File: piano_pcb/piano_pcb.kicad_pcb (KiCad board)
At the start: 2 copper layers, 115 x 85 mm, 28 parts, among them J1 DIN-6, J2 DIN-6, J3 Conn_02x06_Odd_Even, J4 Arduino-NANO-33, J5 SWD, J6 Conn_02x01, U1 TB6612FNG, U2 CN3302_module, U3 battery_holder, U4 MCP1700-1202E_TO92

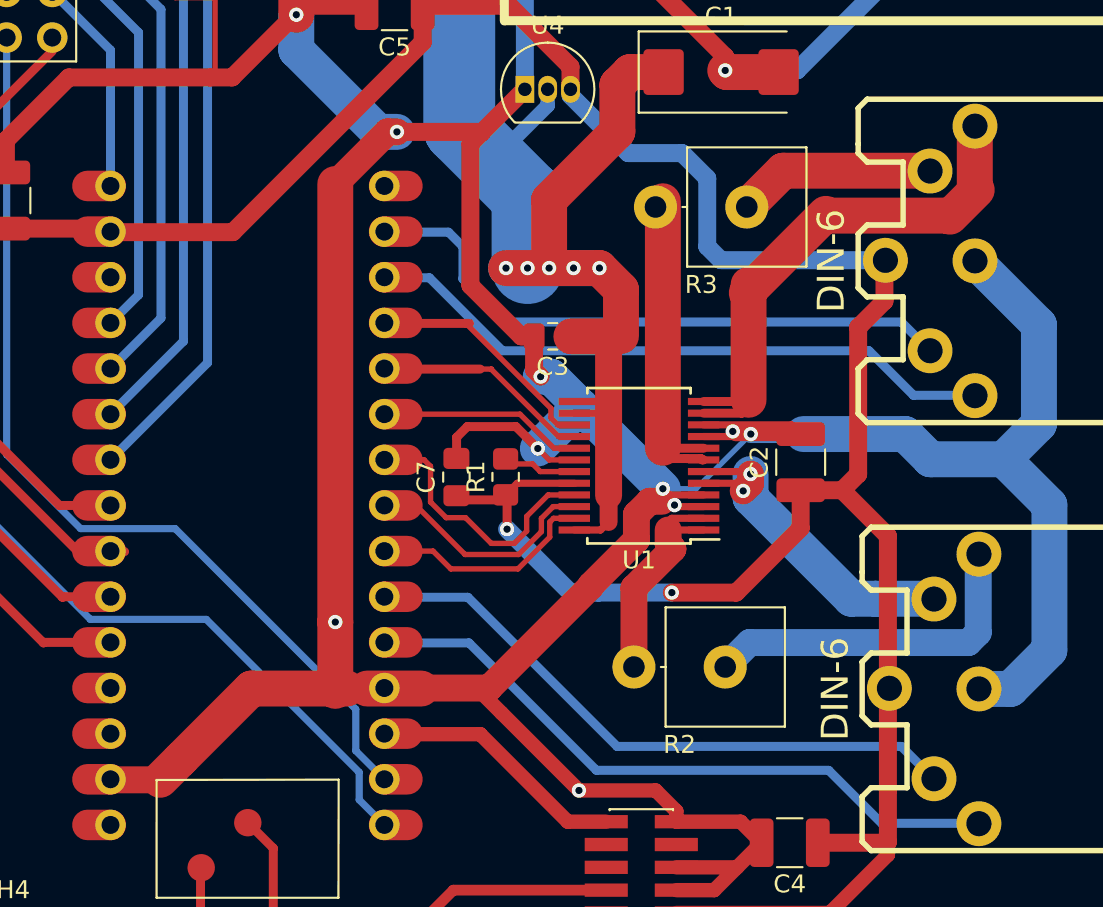
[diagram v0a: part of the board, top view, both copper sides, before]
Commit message: Updated schematics, NOT PCB
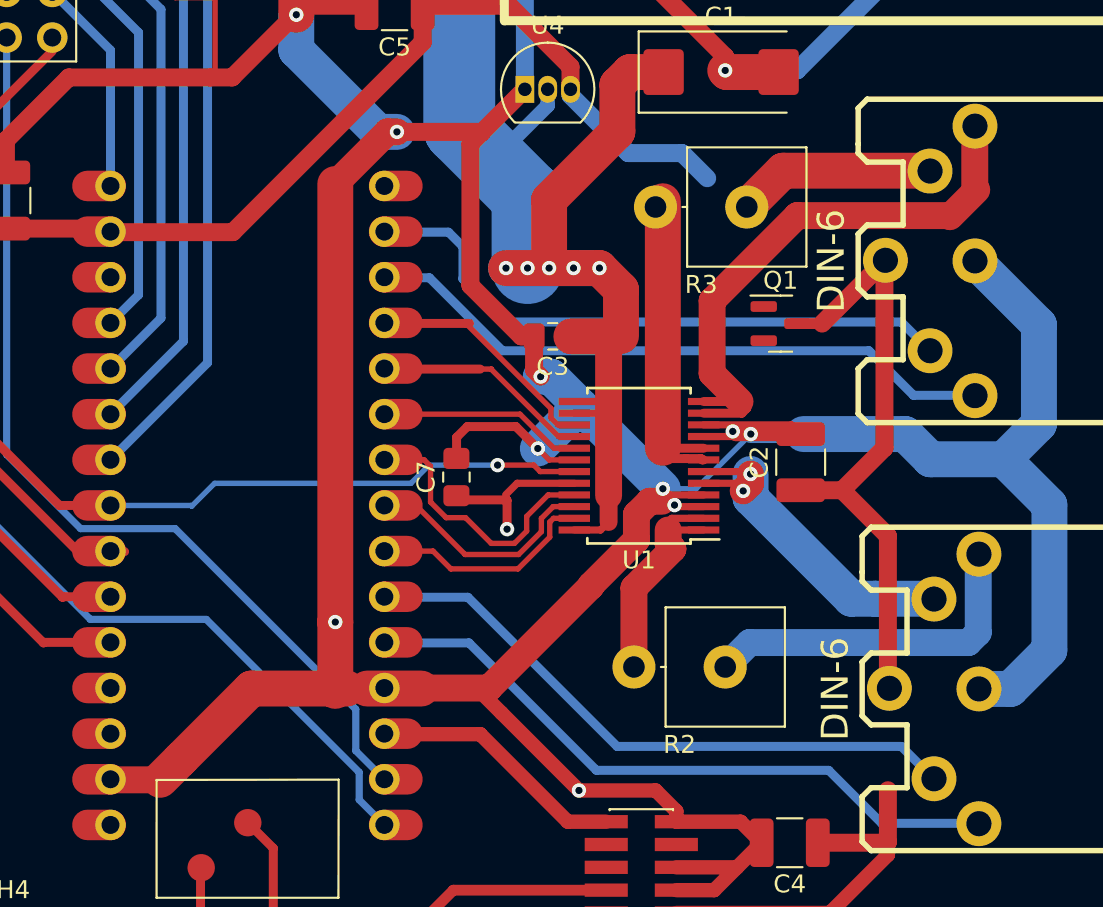
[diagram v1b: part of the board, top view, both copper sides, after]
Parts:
- removed R1: 10k, Resistor_SMD:R_0805_2012Metric_Pad1.20x1.40mm_HandSolder
- added Q1: FDN340P, Package_TO_SOT_SMD:SOT-23, F.Cu at (182.9, 110.5)
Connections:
- C2 pad 1: +3V3 -> Net-(J1-Pad3)
- J1 pad 3: +3V3 -> Net-(J1-Pad3)
- J2 pad 3: +3V3 -> Net-(J1-Pad3)
- J3 pad 12: Net-(J3-Pad12) -> /Controller/stby
- J4 pad 12: Net-(J4-Pad12) -> unconnected-(J4-Pad12)
- J4 pad 13: Net-(J4-Pad13) -> unconnected-(J4-Pad13)
- J4 pad 15: Net-(J4-Pad15) -> unconnected-(J4-Pad15)
- J4 pad 3: Net-(J4-Pad3) -> unconnected-(J4-Pad3)
- J4 pad 30: Net-(J4-Pad30) -> /Controller/EncV3.3
- J4 pad 8: Net-(J3-Pad12) -> /Controller/stby
- J5 pad 6: Net-(J5-Pad6) -> unconnected-(J5-Pad6)
- J5 pad 7: Net-(J5-Pad7) -> unconnected-(J5-Pad7)
- J5 pad 8: Net-(J5-Pad8) -> unconnected-(J5-Pad8)
- U1 pad 19: Net-(R1-Pad2) -> /Controller/stby
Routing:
- net +3V3: track 175.9 -> 106.7 mm, vias 3 -> 2
- net /Controller/stby: track 0.00 -> 61.0 mm, vias 0 -> 1
- net Net-(J1-Pad3): track 0.00 -> 34.8 mm
- net Net-(J3-Pad12): track 34.1 -> 0.00 mm
- net Net-(R1-Pad2): track 3.95 -> 0.00 mm
- net Net-(J1-Pad1): track 30.0 -> 32.1 mm

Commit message: Updated firmware and app
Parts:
- added J7: Conn_01x02, TerminalBlock_Altech:Altech_AK300_1x02_P5.00mm_45-Degree, F.Cu at (155.0, 73.7)
- C1: value 100u -> 10u
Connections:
- C2 pad 1: Net-(J1-Pad3) -> +3V3
- J1 pad 3: Net-(J1-Pad3) -> Net-(Q1-D)
- J2 pad 3: Net-(J1-Pad3) -> Net-(Q1-D)
- Q1 pad 3: Net-(J1-Pad3) -> Net-(Q1-D)
- U2 pad 2: /Controller/Bat -> Net-(J7-Pin_1)
- U3 pad 3: /Controller/Bat -> Net-(J7-Pin_1)
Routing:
- net GND: track 443.3 -> 250.6 mm, vias 11 -> 8
- net /Controller/Bat: track 143.0 -> 19.2 mm, vias 6 -> 0
- net Net-(J1-Pad3): track 34.8 -> 0.00 mm
- net +3V3: track 106.7 -> 141.5 mm
- removed copper zone on B.Cu, net GND

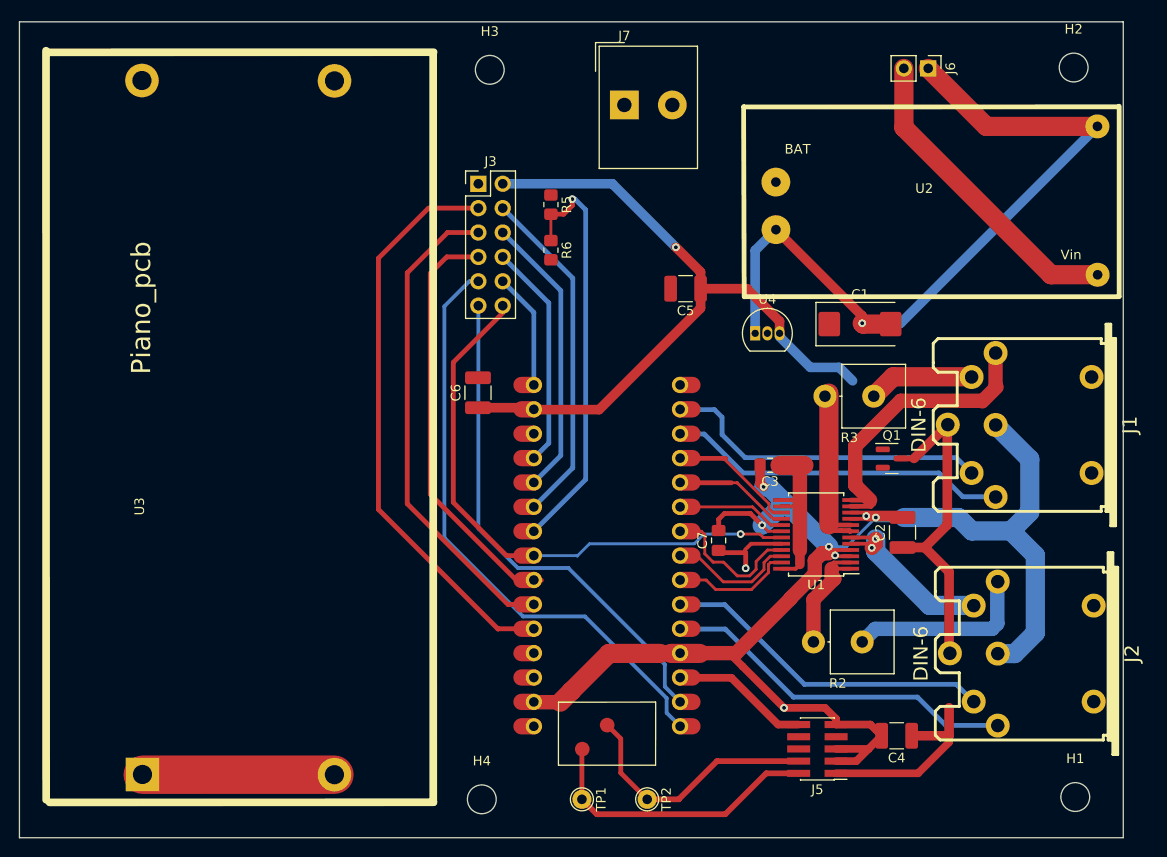
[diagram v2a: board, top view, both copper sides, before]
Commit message: Optimized for low power
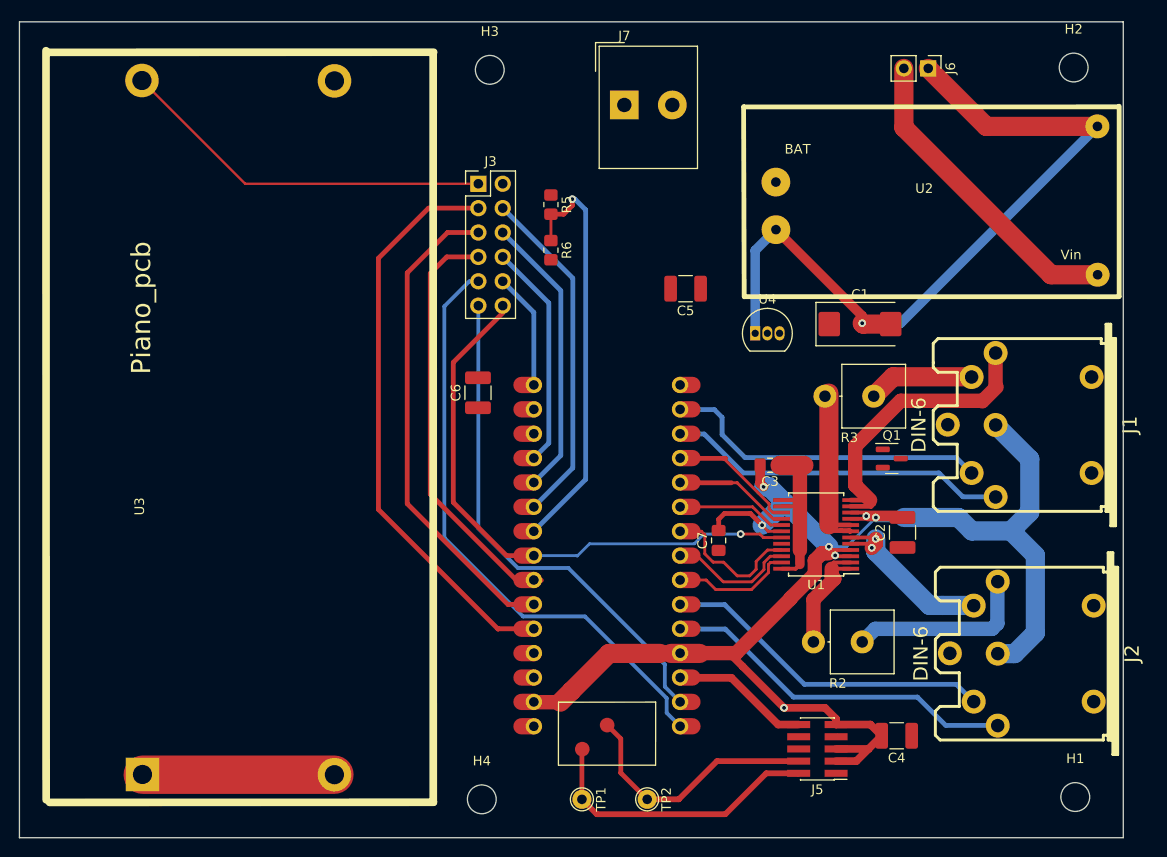
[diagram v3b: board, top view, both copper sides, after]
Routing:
- net +3V3: track 141.5 -> 0.00 mm, vias 2 -> 0
- net GND: track 250.6 -> 290.1 mm

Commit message: PCB to version 2.0
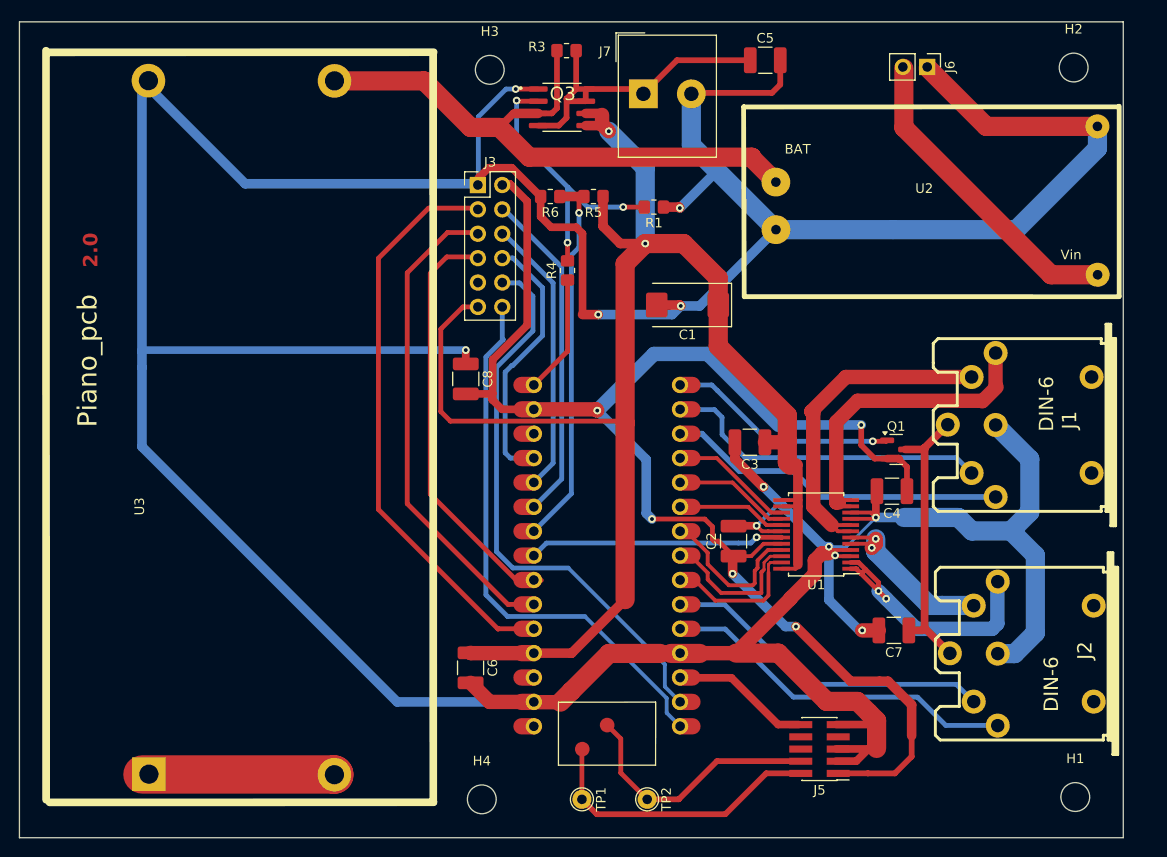
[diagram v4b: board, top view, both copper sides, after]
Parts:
- removed R2: 1, Resistor_THT:R_Axial_Power_L20.0mm_W6.4mm_P5.08mm_Vertical
- removed U4: MCP1700-1202E_TO92, Package_TO_SOT_THT:TO-92_Inline
- added C8: 100n, Capacitor_SMD:C_1210_3225Metric_Pad1.33x2.70mm_HandSolder, F.Cu at (138.5, 102.2)
- added Q3: IRF7319, library:SOIC127P600X175-8N, F.Cu at (148.5, 73.9)
- added R1: 10k, Resistor_SMD:R_0805_2012Metric_Pad1.20x1.40mm_HandSolder, F.Cu at (158.1, 84.3)
- added R4: 100, Resistor_SMD:R_0805_2012Metric_Pad1.20x1.40mm_HandSolder, F.Cu at (149.1, 90.9)
- C1: footprint Capacitor_Tantalum_SMD:CP_EIA-7343-30_AVX-N_Pad2.25x2.55mm_HandSolder -> Capacitor_Tantalum_SMD:CP_EIA-7343-30_AVX-N_HandSolder
- C3, C7: footprint Capacitor_SMD:C_0805_2012Metric_Pad1.18x1.45mm_HandSolder -> Capacitor_SMD:C_1210_3225Metric_Pad1.33x2.70mm_HandSolder
- C4, C6: value 10u -> 100n
- C5: value 10u -> 10n
- J1, J2: footprint myAV:din-6-1cm -> library:din-6-1cm
- J4: footprint myAV:NANO_33_BLE -> library:NANO_33_BLE
- R3: value 1 -> 100k; footprint Resistor_THT:R_Axial_Power_L20.0mm_W6.4mm_P5.08mm_Vertical -> Resistor_SMD:R_0805_2012Metric_Pad1.20x1.40mm_HandSolder
- R5: value 470k -> 220k
- R6: value 330k -> 150k
- U1: footprint myAV:SSOP-24_5.3x8.2mm_P0.65mm -> library:SSOP-24_5.3x8.2mm_P0.65mm
- U2: footprint myAV:CN3302-FP -> library:CN3302-FP
- U3: footprint myAV:Battery_2x_18650 -> library:Battery_2x_18650
- moved R3 48.2 mm to (149.0, 68.0)
- moved C6 28.7 mm to (139.0, 132.3), turned to -90 degrees
- moved C4 25.5 mm to (182.9, 113.9)
- moved C5 25.2 mm to (169.7, 69.0), turned to 0 degrees
- moved C7 20.5 mm to (183.1, 128.4), turned to 180 degrees
- moved C1 18.1 mm to (161.6, 94.5), turned to 180 degrees
- moved C2 17.6 mm to (166.4, 119.1)
- moved R6 5.59 mm to (147.3, 83.2), turned to 180 degrees
- moved R5 4.51 mm to (151.8, 83.2), turned to 180 degrees
- moved C3 3.19 mm to (168.1, 108.8)
- moved J7 2.29 mm to (157.0, 72.5)
- moved Q1 1.05 mm to (183.3, 109.5)
- moved J5 0.22 mm to (175.3, 140.8)
- moved J6 0.18 mm to (186.6, 69.7)
- moved J3 0.14 mm to (139.8, 82.0)
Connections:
- C5 pad 1: +3V3 -> Net-(J7-Pin_1)
- C6 pad 1: +3V3 -> /Controller/Bat
- C7 pad 1: +3V3 -> Net-(Q1-D)
- J3 pad 11: Net-(J3-Pin_11) -> /Controller/Bat
- J3 pad 12: /Controller/stby -> Net-(J3-Pin_12)
- J3 pad 9: Net-(J3-Pin_9) -> unconnected-(J3-Pin_9-Pad9)
- J4 pad 1: Net-(J3-Pin_10) -> /Controller/PPio
- J4 pad 12: unconnected-(J4-Pad12) -> /Controller/Bat
- J4 pad 16: Net-(J3-Pin_9) -> Net-(J3-Pin_12)
- J4 pad 17: Net-(J3-Pin_11) -> Net-(J3-Pin_10)
- J7 pad 2: /Controller/Bat -> GND
- R3 pad 1: Net-(J1-Pad2) -> Net-(J7-Pin_1)
- R3 pad 2: Net-(R3-Pad2) -> Net-(U2-BAT)
- U1 pad 1: Net-(R2-Pad2) -> Net-(J2-Pad1)
- U1 pad 2: Net-(R2-Pad2) -> Net-(J2-Pad1)
- U1 pad 7: Net-(R3-Pad2) -> Net-(J1-Pad2)
- U1 pad 8: Net-(R3-Pad2) -> Net-(J1-Pad2)
- U2 pad 2: Net-(J7-Pin_1) -> Net-(U2-BAT)
- U3 pad 3: Net-(J7-Pin_1) -> Net-(U2-BAT)
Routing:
- net GND: track 290.1 -> 516.0 mm, vias 8 -> 11
- net +3V3: track 0.00 -> 153.8 mm, vias 0 -> 5
- net /Controller/Bat: track 19.2 -> 168.2 mm, vias 0 -> 2
- net Net-(U2-BAT): track 0.00 -> 63.2 mm
- net Net-(J3-Pin_9): track 62.3 -> 0.00 mm
- net Net-(J3-Pin_12): track 0.00 -> 58.3 mm
- net Net-(J3-Pin_11): track 53.1 -> 0.00 mm
- net Net-(J3-Pin_10): track 12.1 -> 58.9 mm
- net /Controller/stby: track 61.0 -> 28.0 mm
- net Net-(J7-Pin_1): track 0.00 -> 32.3 mm
- net Net-(Q3-Pad2): track 0.00 -> 30.2 mm, vias 0 -> 3
- net Net-(Q1-D): track 0.00 -> 29.8 mm
- net Net-(J1-Pad2): track 11.0 -> 35.1 mm
- net /Controller/EncV3.3: track 0.00 -> 24.0 mm, vias 0 -> 1
- net Net-(R3-Pad2): track 18.5 -> 0.00 mm
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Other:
- board text added: "2.0"

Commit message: Updated and added 3d picture
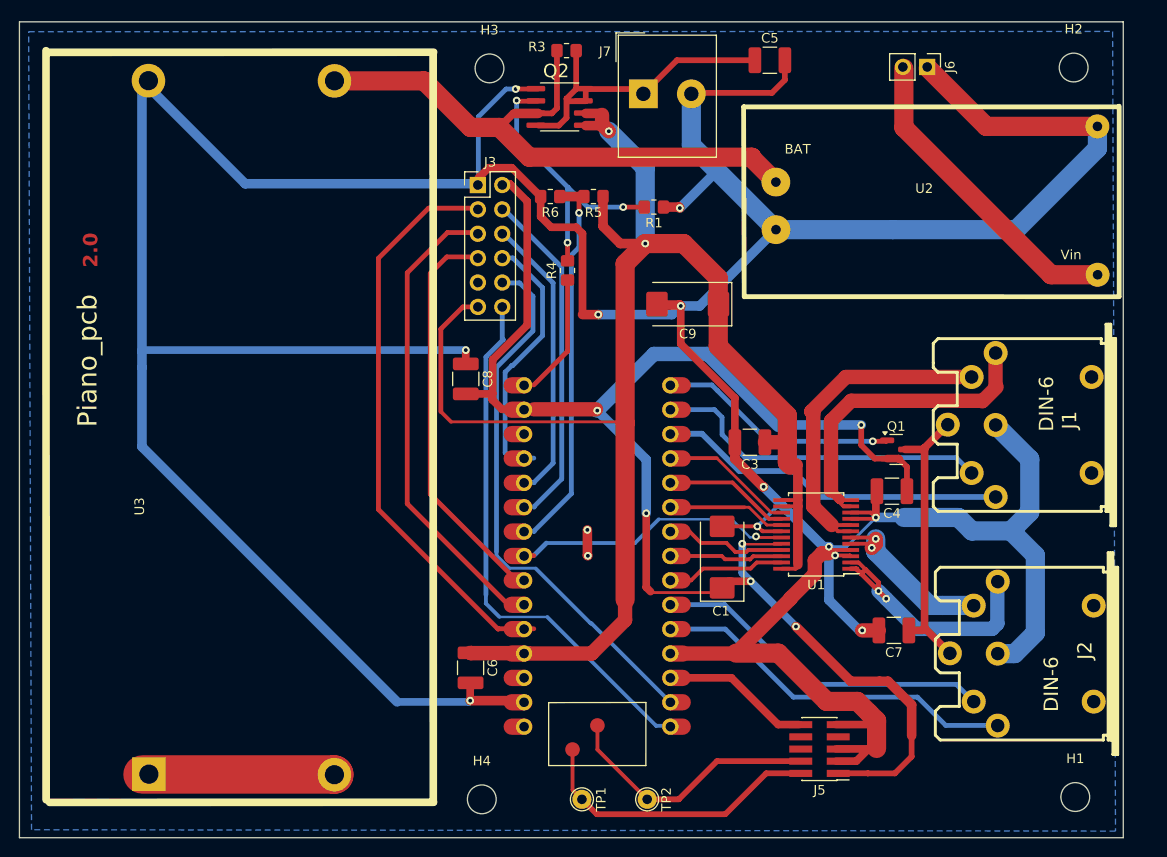
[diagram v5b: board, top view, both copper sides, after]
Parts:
- removed C2: 10u, Capacitor_SMD:C_1210_3225Metric_Pad1.33x2.70mm_HandSolder
- removed J4: Arduino-NANO-33, library:NANO_33_BLE
- removed Q3: IRF7319, library:SOIC127P600X175-8N
- added C9: 10u, Capacitor_Tantalum_SMD:CP_EIA-7343-30_AVX-N_HandSolder, F.Cu at (161.6, 94.4)
- added J8: Arduino-NANO-33, library:NANO_33_BLE, F.Cu at (152.2, 120.7)
- added Q2: IRF7319, library:SOIC127P600X175-8N, F.Cu at (148.3, 73.9)
- moved C1 26.5 mm to (165.2, 120.8), turned to 90 degrees
- moved C5 0.48 mm to (170.2, 69.0)
- moved H3 0.15 mm to (141.0, 69.8)
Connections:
- net Net-(J7-Pin_1) renamed /Power/Vgate
- C1 pad 1: /Controller/Bat -> +3.3V
- C4 pad 1: +3V3 -> +3.3V
- C8 pad 2: +3V3 -> +3.3V
- J3 pad 2: +3V3 -> +3.3V
- J5 pad 1: +3V3 -> +3.3V
- Q1 pad 2: +3V3 -> +3.3V
- U1 pad 20: +3V3 -> +3.3V
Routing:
- net +3.3V: track 0.00 -> 159.9 mm, vias 0 -> 6
- net +3V3: track 153.8 -> 0.00 mm, vias 5 -> 0
- net GND: track 516.0 -> 506.1 mm, vias 11 -> 14
- net /Controller/ain2: track 17.0 -> 11.3 mm
- net /Controller/ain1: track 16.6 -> 11.9 mm
- net Net-(J3-Pin_7): track 45.8 -> 41.4 mm
- net /Controller/pwma: track 14.4 -> 11.8 mm
- net /Controller/Bat: track 168.2 -> 170.7 mm
- net Net-(J1-Pad1): track 34.4 -> 32.3 mm
- net Net-(J3-Pin_10): track 58.9 -> 56.8 mm
- net /Controller/stby: track 28.0 -> 29.7 mm
- net Net-(J3-Pin_12): track 58.3 -> 57.0 mm
- net /Controller/bin1: track 10.7 -> 11.7 mm
- added copper zone on B.Cu, net GND
